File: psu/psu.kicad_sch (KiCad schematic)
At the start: 21 parts, among them J1 Conn_01x02_Socket, J2 Conn_01x03_Socket, U1 L7812, U2 L7912

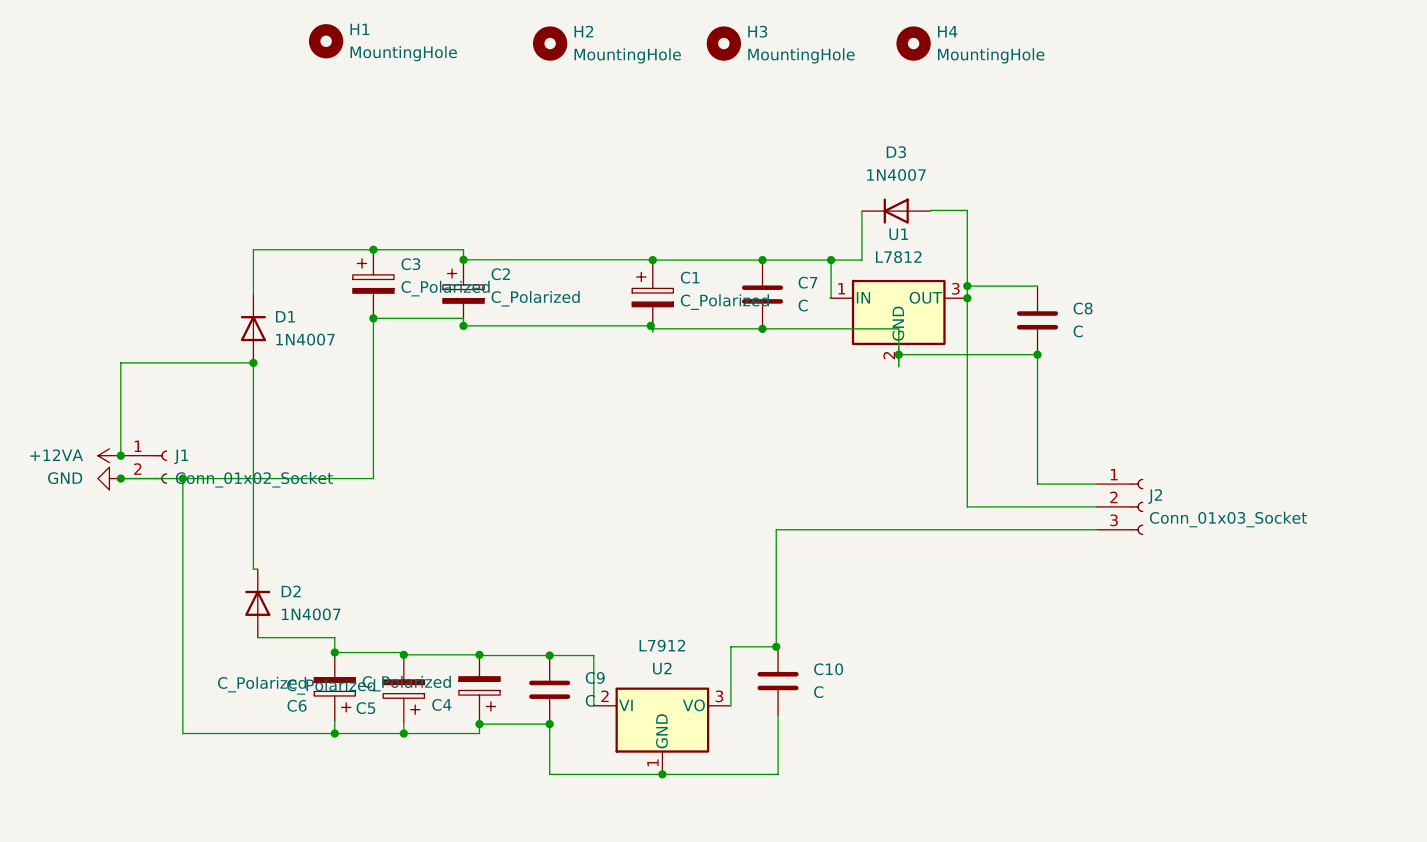
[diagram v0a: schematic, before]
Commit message: add psu bom, improve trace width
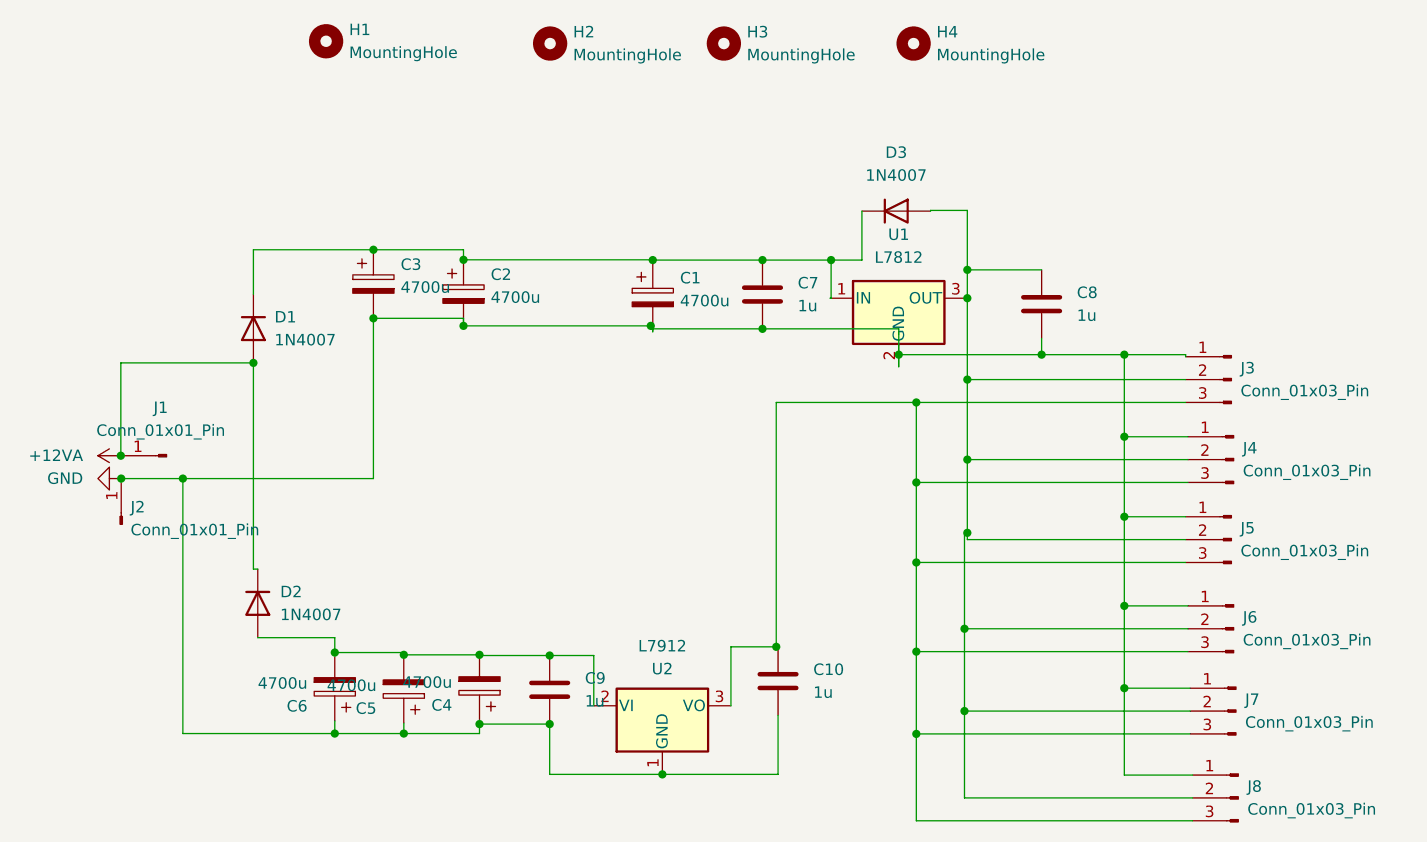
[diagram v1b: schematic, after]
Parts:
- removed J1: Conn_01x02_Socket, Connector_PinSocket_2.54mm:PinSocket_1x02_P2.54mm_Vertical, symbol Connector:Conn_01x02_Socket
- removed J2: Conn_01x03_Socket, Connector_PinSocket_2.54mm:PinSocket_1x03_P2.54mm_Vertical, symbol Connector:Conn_01x03_Socket
- added J1, J2: Conn_01x01_Pin, Connector_PinHeader_2.54mm:PinHeader_1x01_P2.54mm_Vertical, symbol Connector:Conn_01x01_Pin
- added J3, J4, J5, J6, J7, J8: Conn_01x03_Pin, Connector_PinHeader_2.54mm:PinHeader_1x03_P2.54mm_Vertical, symbol Connector:Conn_01x03_Pin
- C1, C2, C3, C4, C5, C6: value C_Polarized -> 4700u
- C10, C7, C8, C9: value C -> 1u; footprint Capacitor_THT:C_Axial_L3.8mm_D2.6mm_P7.50mm_Horizontal -> Capacitor_THT:C_Disc_D4.3mm_W1.9mm_P5.00mm
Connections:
- net +12VA: now also J1.1 (Pin_1)
- net GND: now also J2.1 (Pin_1), J3.1 (Pin_1), J4.1 (Pin_1), J5.1 (Pin_1), J6.1 (Pin_1), J7.1 (Pin_1), J8.1 (Pin_1)
- net at C8.1, D3.2 (A), U1.3 (OUT): now also J3.2 (Pin_2), J4.2 (Pin_2), J5.2 (Pin_2), J6.2 (Pin_2), J7.2 (Pin_2), J8.2 (Pin_2)
- net at C10.1, U2.3 (VO): now also J3.3 (Pin_3), J4.3 (Pin_3), J5.3 (Pin_3), J6.3 (Pin_3), J7.3 (Pin_3), J8.3 (Pin_3)
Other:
- moved on the sheet: C8
